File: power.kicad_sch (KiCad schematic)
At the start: 43 parts, among them J3 Conn_02x02_Counter_Clockwise, Q7 Q_NMOS, Q8 Q_NMOS, U2 TPS5430DDA, U3 TPS2121, U4 LDL212PV33R, U7 TPS56A37

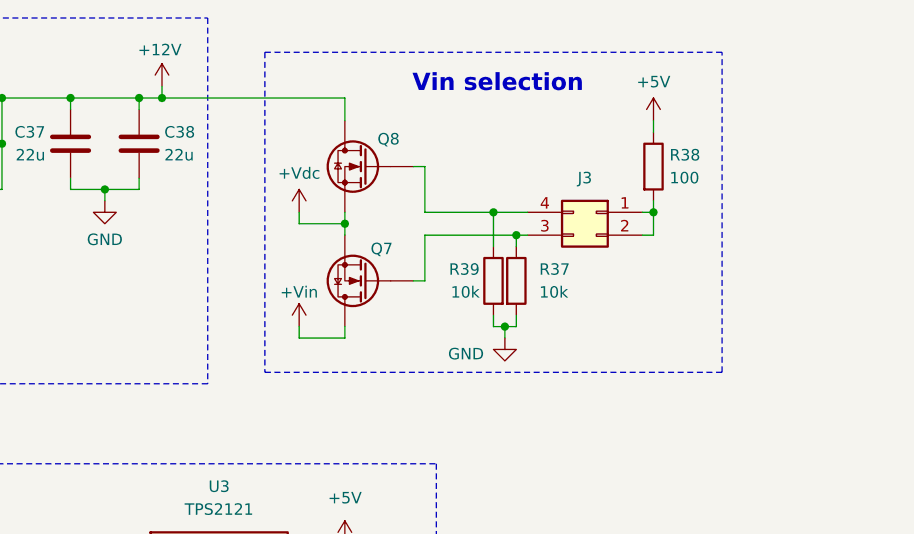
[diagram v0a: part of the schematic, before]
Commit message: schem: changed selection circuit to back to back fets
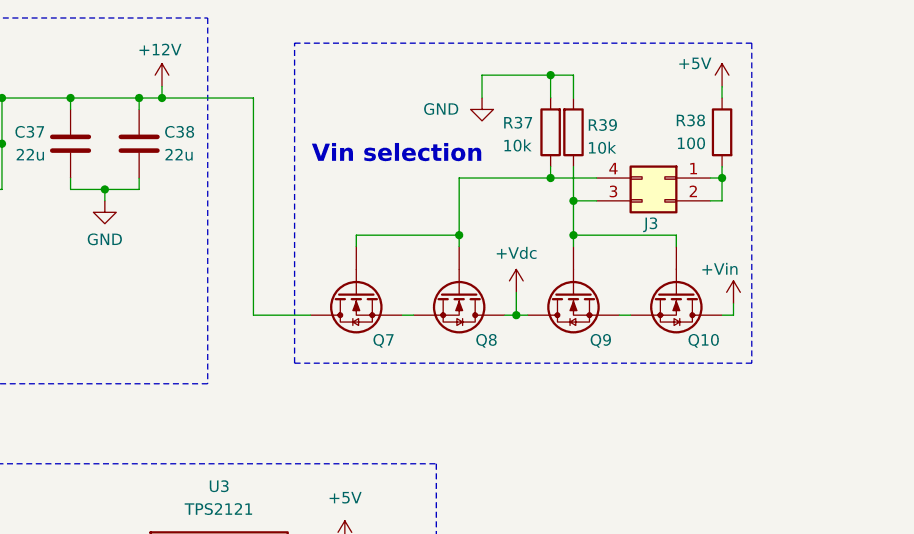
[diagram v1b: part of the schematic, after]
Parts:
- added Q10, Q9: Q_NMOS, symbol Device:Q_NMOS
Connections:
- net +12V: now also Q7.D; no longer Q8.D
- net +Vdc: now also Q8.D, Q9.D; no longer Q7.S, Q8.S
- net +Vin: now also Q10.D; no longer Q7.D
- net at J3.4 (Pin_4), Q8.G: now also Q7.G, R37.1; no longer R39.1
- new net: J3.3 (Pin_3), Q10.G, Q9.G, R39.1
- new net: Q10.S, Q9.S
- new net: Q7.S, Q8.S
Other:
- moved on the sheet: J3, R37, R38, R39

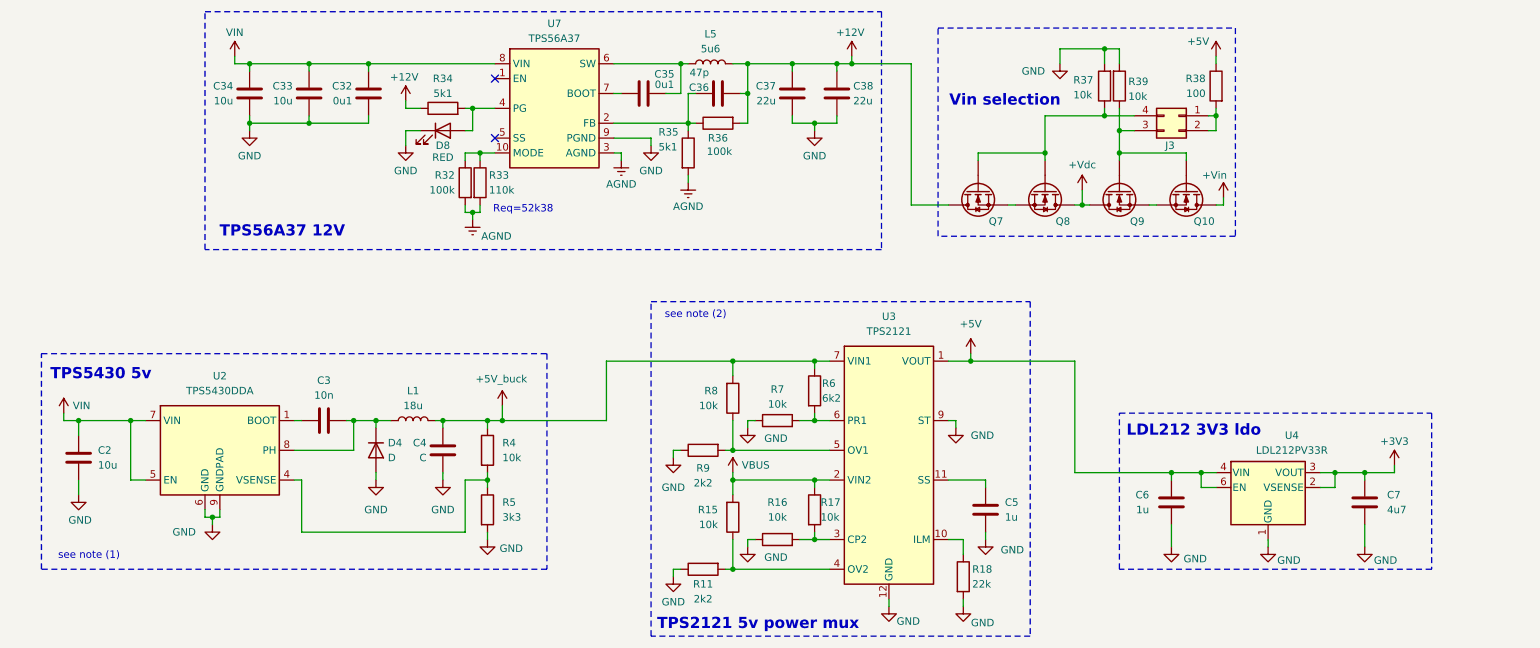
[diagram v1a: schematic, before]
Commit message: schem: add 3v reference
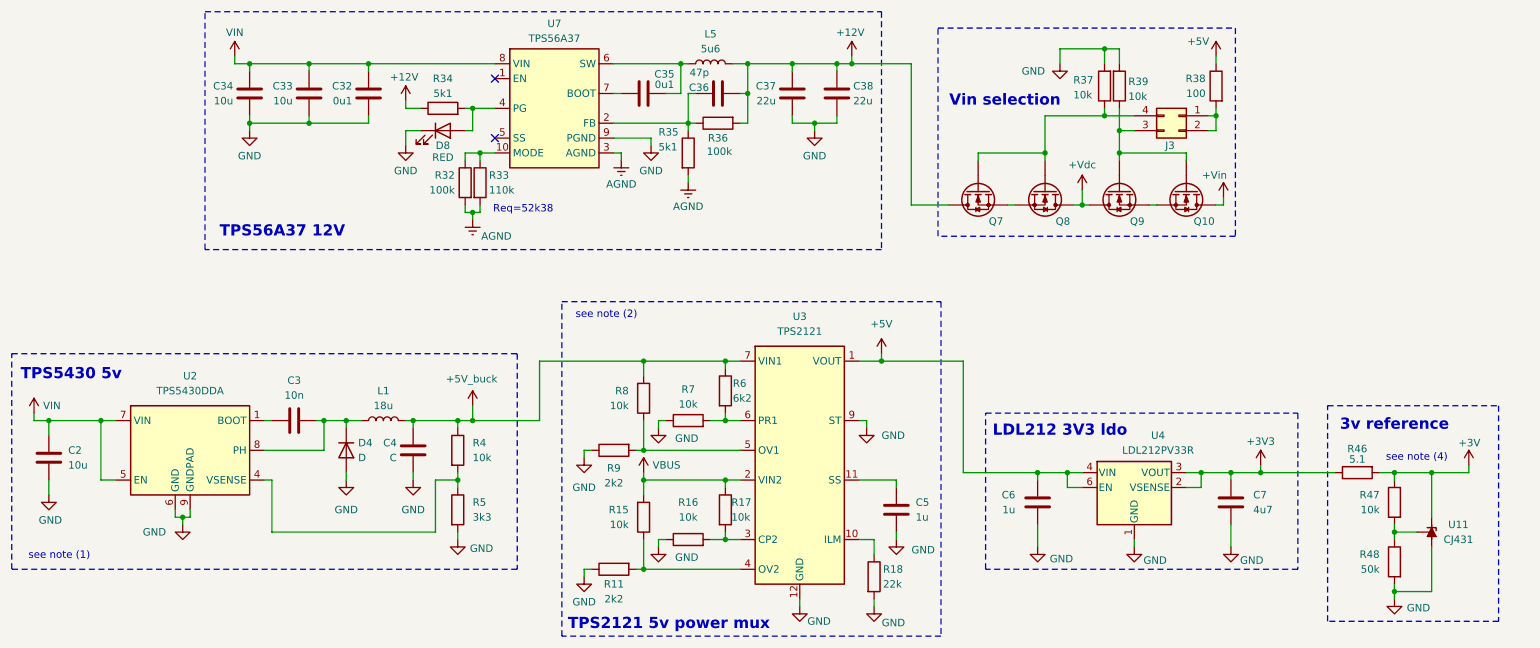
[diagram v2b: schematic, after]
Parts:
- added R46: 5.1, Resistor_SMD:R_0805_2012Metric, symbol Device:R
- added R47: 10k, Resistor_SMD:R_0603_1608Metric, symbol Device:R
- added R48: 50k, Resistor_SMD:R_0603_1608Metric, symbol Device:R
- added U11: CJ431, Package_TO_SOT_SMD:SOT-23, symbol Pers:CJ431
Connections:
- net +3V3: now also R46.1
- net GND: now also R48.2, U11.3 (A)
- new net: R47.2, R48.1, U11.1 (REF)
- new net +3V: R46.2, R47.1, U11.2 (K)
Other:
- note added: "3v reference"
- note added: "see note (4)"
- moved on the sheet: C2, C3, C4, C5, C6, C7, D4, L1, R11, R15, R16, R17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

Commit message: schem: add pins to hierachical sheets
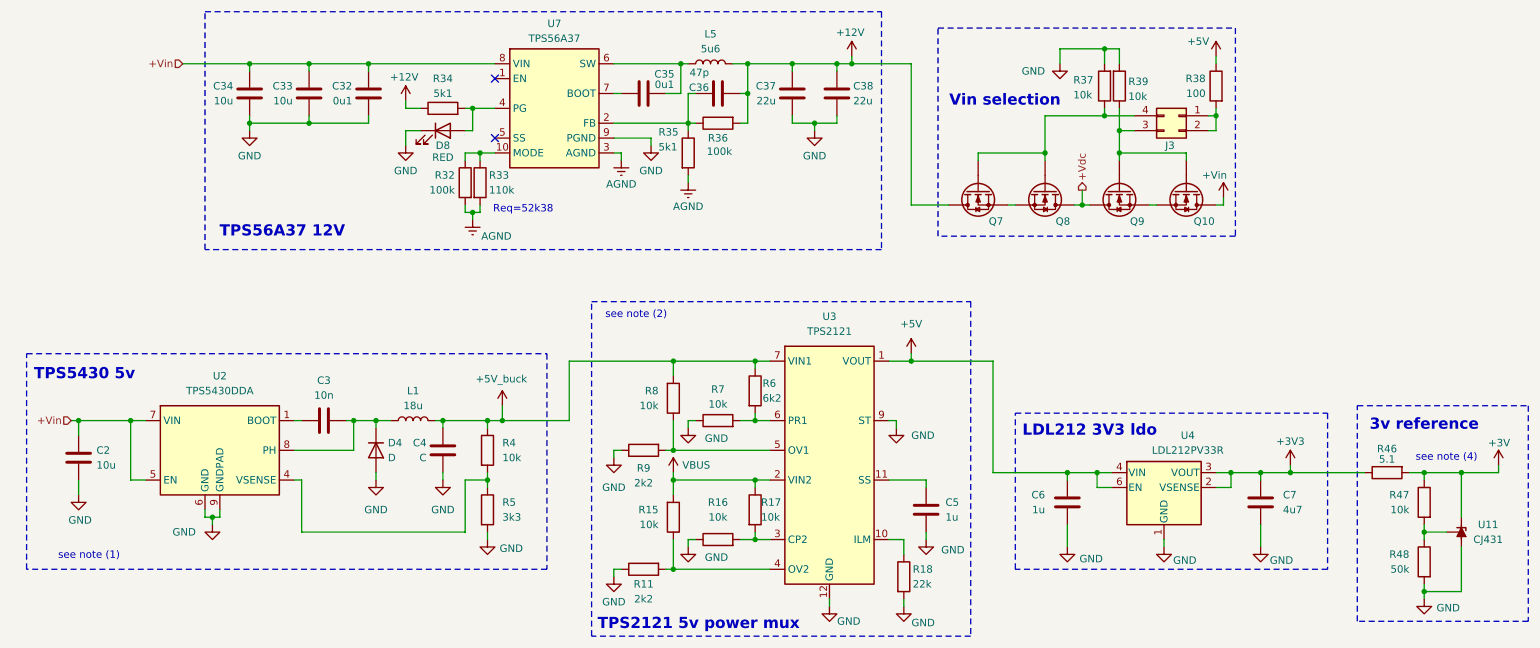
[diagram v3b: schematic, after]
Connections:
- net VIN is gone; now on net +Vin: C2.1, C32.1, C33.1, C34.1, U2.5 (EN), U2.7 (VIN), U7.8 (VIN)
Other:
- moved on the sheet: C2, C3, C4, C5, C6, C7, D4, L1, R11, R15, R16, R17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

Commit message: schem: add +Vbus to hierachical
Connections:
- net VBUS renamed +Vbus
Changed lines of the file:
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@@
 	(wire
 		(pts
+			(xy 130.81 104.14) (xy 129.54 104.14)
+		)
+		(stroke
+			(width 0)
+			(type default)
+		)
+	)
+	(wire
+		(pts
 			(xy 128.27 121.92) (xy 129.54 121.92)
 		)
@@
 	(wire
 		(pts
-			(xy 129.54 105.41) (xy 129.54 106.68)
+			(xy 129.54 104.14) (xy 129.54 106.68)
 		)
 		(stroke
@@
 		)
 	)
+	(hierarchical_label "+Vbus"
+		(shape input)
+		(at 130.81 104.14 0)
+		(effects
+			(font
+				(size 1.27 1.27)
+			)
+			(justify left)
+		)
+	)
 	(hierarchical_label "+Vdc"
 		(shape output)
@@
 					(unit 1)
 				)
-			)
-		)
-	)
-	(symbol
-		(lib_id "power:VBUS")
-		(at 129.54 105.41 0)
-		(mirror y)
-		(unit 1)
-		(exclude_from_sim no)
-		(in_bom yes)
-		(on_board yes)
-		(dnp no)
-		(property "Reference" "#PWR032"
-			(at 129.54 109.22 0)
-			(effects
-				(font
-					(size 1.27 1.27)
-				)
-				(hide yes)
-			)
-		)
-		(property "Value" "VBUS"
-			(at 131.064 104.14 0)
-			(effects
-				(font
-					(size 1.27 1.27)
-				)
-				(justify right)
-			)
-		)
-		(property "Footprint" ""
-			(at 129.54 105.41 0)
-			(effects
-				(font
-					(size 1.27 1.27)
-				)
-				(hide yes)
-			)
-		)
-		(property "Datasheet" ""
-			(at 129.54 105.41 0)
-			(effects
-				(font
-					(size 1.27 1.27)
-				)
-				(hide yes)
-			)
-		)
-		(property "Description" "Power symbol creates a global label with name \"VBUS\""
-			(at 129.54 105.41 0)
-			(effects
-				(font
-					(size 1.27 1.27)
-				)
-				(hide yes)
-			)
-		)
-		(pin "1"
-		)
-		(instances
-			(project "power"
-				(path "/1e5fa1ef-e283-4594-971e-80ab15cefa9e"
-					(reference "#PWR?")
-					(unit 1)
-				)
-			)
-			(project "motor-power-poc"
-				(path "/a1dc4c9e-7b20-4b66-a693-9133bc644c6b/c6ffff07-df24-4c45-882d-f55b522e3469"
-					(reference "#PWR032")
-					(unit 1)
-				)

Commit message: schem: add +5V to hierachical
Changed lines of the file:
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@@
+	)
+	(junction
+		(at 184.15 86.36)
+		(diameter 0)
+		(color 0 0 0 0)
 	)
 	(junction
@@
 		(pts
 			(xy 120.65 101.6) (xy 119.38 101.6)
+		)
+		(stroke
+			(width 0)
+			(type default)
+		)
+	)
+	(wire
+		(pts
+			(xy 184.15 86.36) (xy 186.69 86.36)
 		)
 		(stroke
@@
 		(effects
 			(font
+				(size 1.27 1.27)
+			)
+			(justify left)
+		)
+	)
+	(hierarchical_label "+5V"
+		(shape output)
+		(at 186.69 86.36 0)
+		(effects
+			(font

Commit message: schem: add test points
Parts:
- added TP1, TP2, TP3, TP4, TP5, TP9: TestPoint, symbol Connector:TestPoint
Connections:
- net +12V: now also TP1.1
- net +3V: now also TP5.1
- net +3V3: now also TP4.1
- net +5V: now also TP3.1
- net +5V_buck: now also TP2.1
- net +Vdc: now also TP9.1

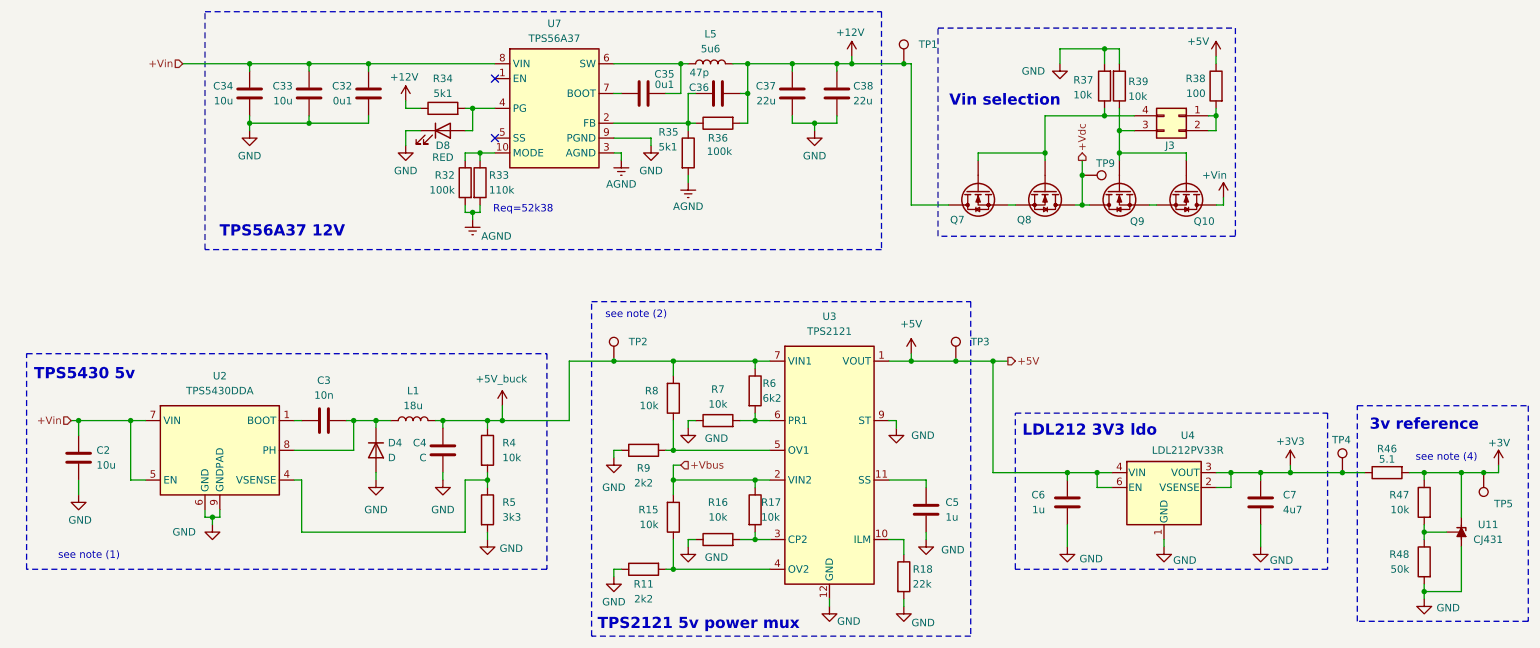
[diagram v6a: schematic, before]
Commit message: schem: renumber
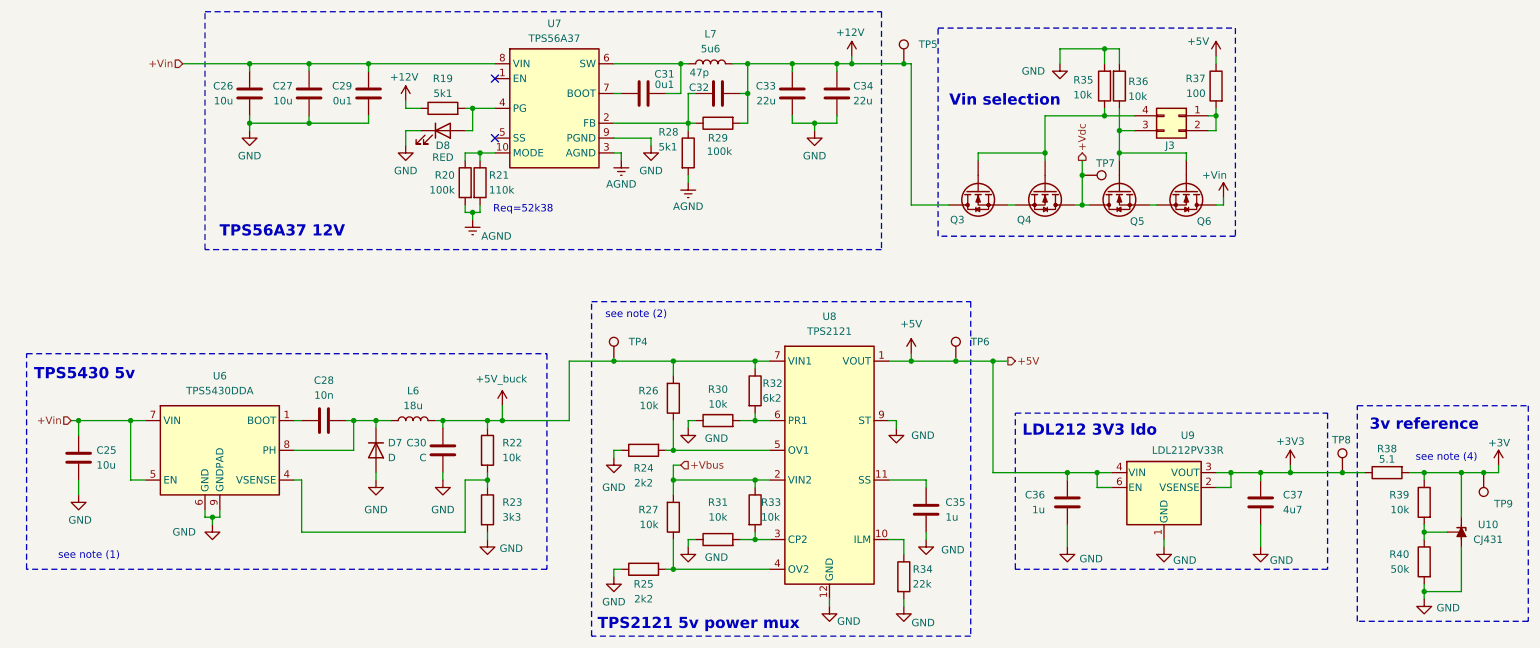
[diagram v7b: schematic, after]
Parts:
- renumbered C2 to C25, C34 to C26, C33 to C27, C3 to C28, C32 to C29, C4 to C30, C35 to C31, C36 to C32, C37 to C33, C38 to C34, C5 to C35, C6 to C36, C7 to C37, D4 to D7, L1 to L6, L5 to L7, Q7 to Q3, Q8 to Q4, Q9 to Q5, Q10 to Q6, R34 to R19, R32 to R20, R33 to R21, R4 to R22, R5 to R23, R9 to R24, R11 to R25, R8 to R26, R15 to R27, R35 to R28, R36 to R29, R7 to R30, R16 to R31, R6 to R32, R17 to R33, R18 to R34, R37 to R35, R39 to R36, R38 to R37, R46 to R38, R47 to R39, R48 to R40, TP2 to TP4, TP1 to TP5, TP3 to TP6, TP9 to TP7, TP4 to TP8, TP5 to TP9, U11 to U10, U2 to U6, U3 to U8, U4 to U9

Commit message: schem: run and fix ERC
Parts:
- U8: symbol Pers:TPS2121 -> GLCS:TPS2121
